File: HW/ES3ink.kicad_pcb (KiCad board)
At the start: 2 copper layers, 60.8 x 31 mm, 77 parts, among them J1 USB_C_Receptacle_USB2.0, J2 Conn_01x24_Pin, J3 Conn_01x02_Pin, J4 Conn_01x04_Socket, J5 USB_C_Receptacle_USB2.0, Q1 AO3401A, Q2 SI1308EDL-T1-GE3, Q3 DMP2045U-7, Q4 SI2305, SW1 RESET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

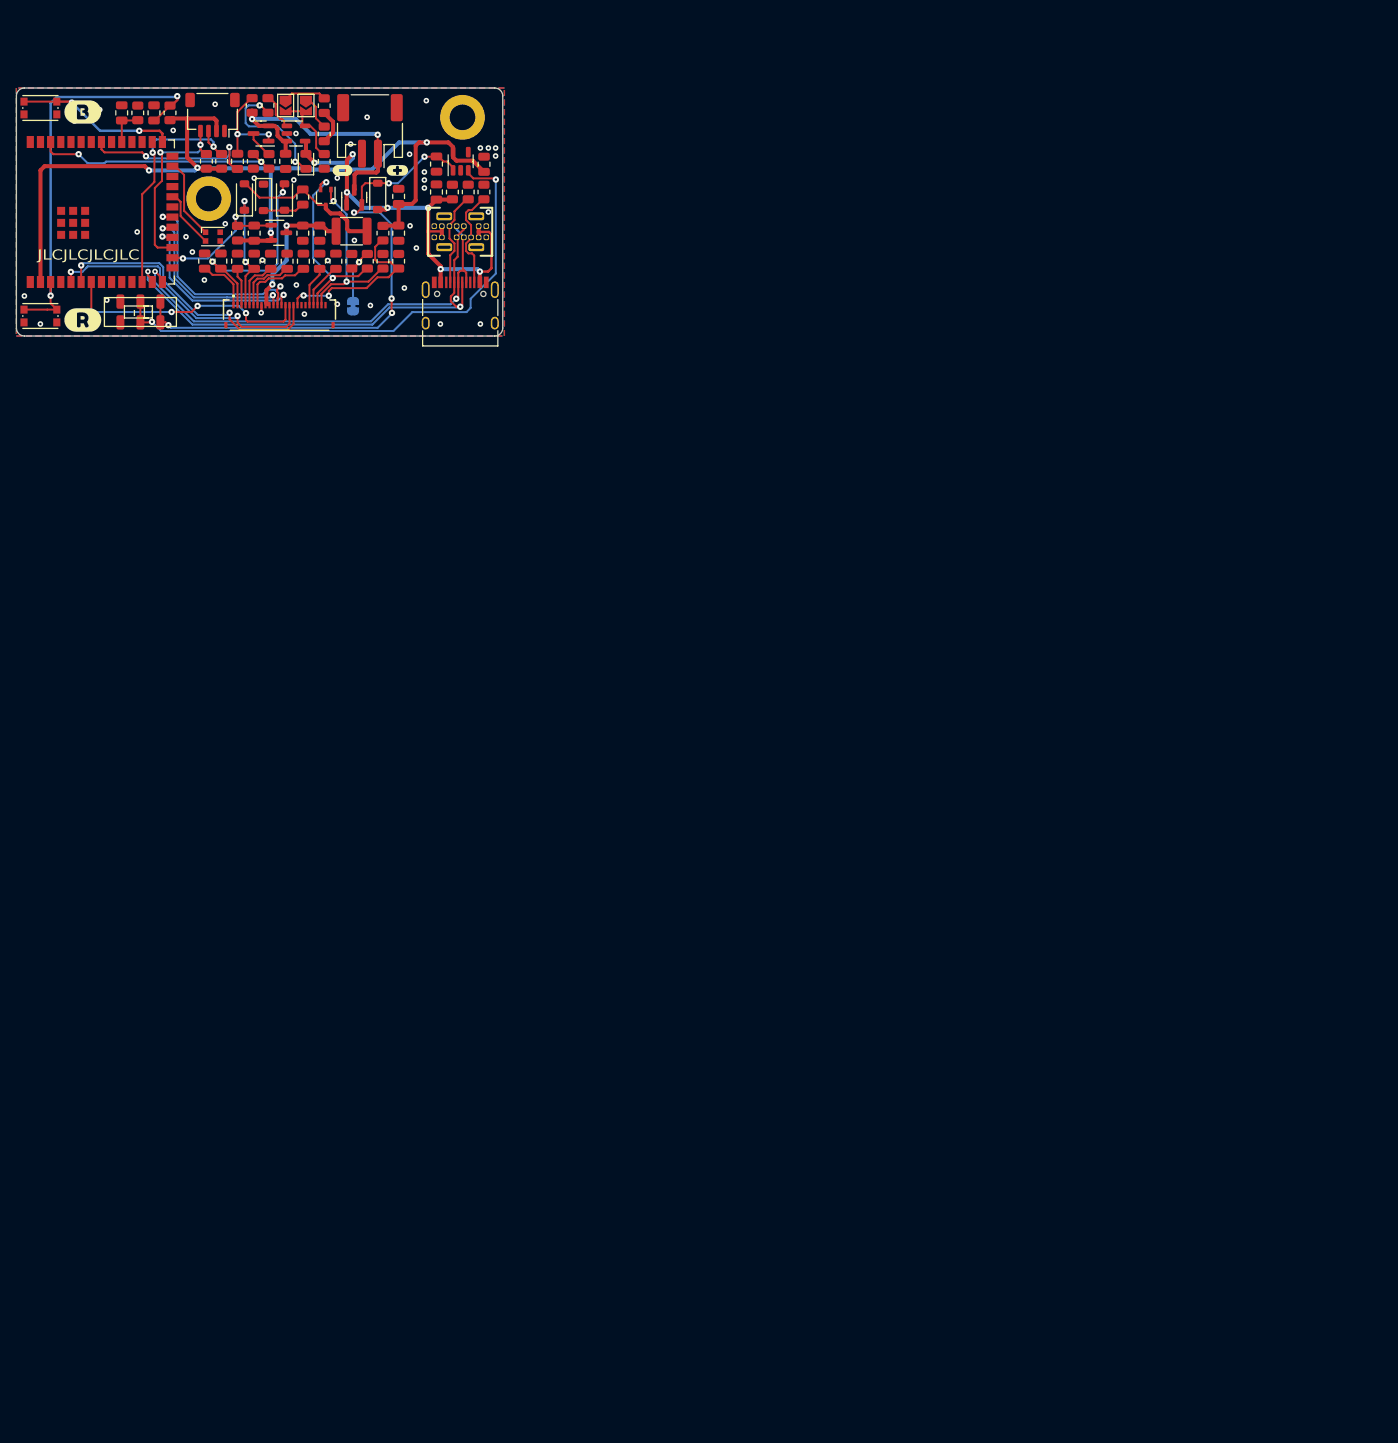
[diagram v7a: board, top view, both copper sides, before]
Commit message: Update to P1.2
- changed e-ink pwr pin to IO3
- unified reference text values
- add link to view design in KiCanvas
- version increment to P1.2
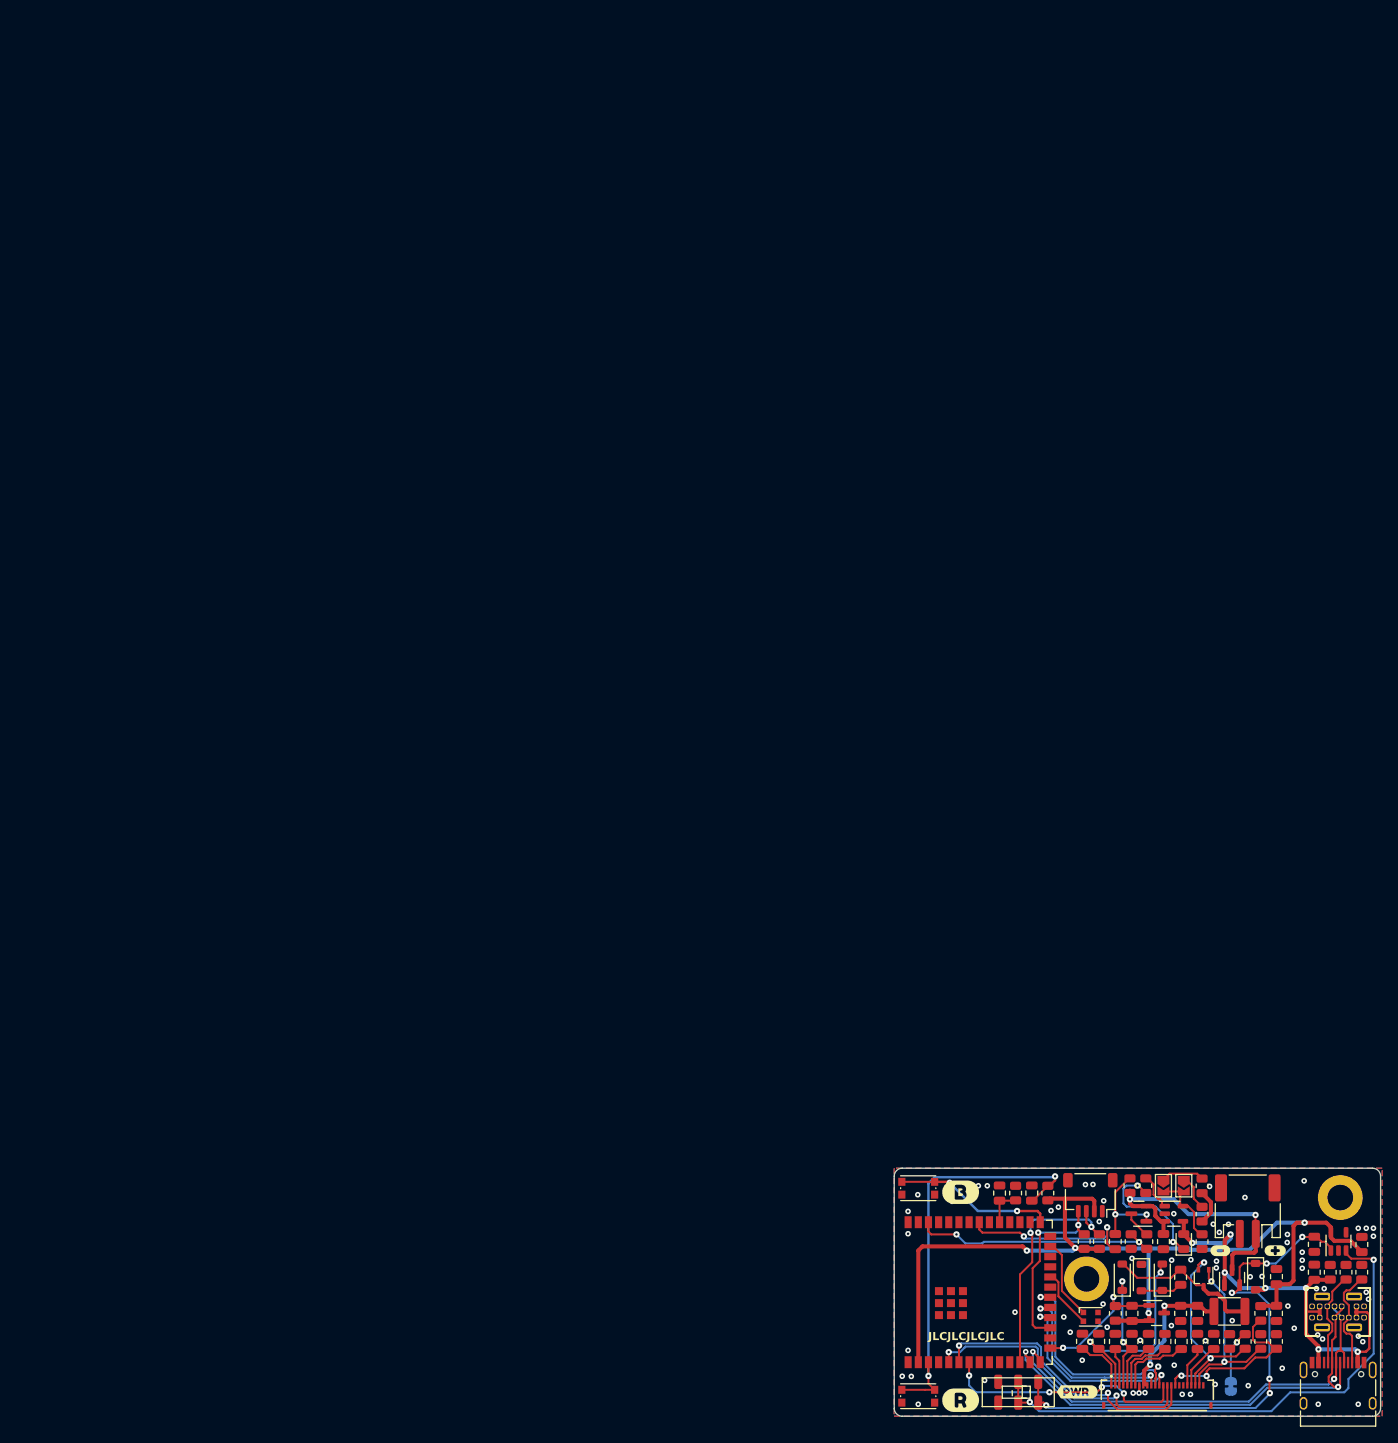
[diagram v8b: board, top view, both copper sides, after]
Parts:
- added kibuzzard-659DC4DE: G***, kibuzzard-659DC4DE, F.Cu at (132.6, 132.0)
- moved C19 174.0 mm to (145.5, 117.7)
- moved C21 174.0 mm to (162.2, 113.5)
- moved D1 174.0 mm to (138.2, 117.7)
- moved D2 174.0 mm to (143.2, 117.7)
- moved D3 174.0 mm to (140.6, 117.7)
- moved D6 174.0 mm to (134.3, 122.6)
- moved G*** 174.0 mm to (142.2, 120.0)
- moved G*** 174.0 mm to (154.1, 120.0)
- moved G*** 174.0 mm to (122.7, 120.0)
- moved J4 174.0 mm to (134.2, 107.4)
- moved Q3 174.0 mm to (152.0, 117.7)
- moved SW2 174.0 mm to (112.7, 106.5)
- moved U1 174.0 mm to (119.7, 119.5)
- moved kibuzzard-649216B3 174.0 mm to (118.0, 107.0)
- moved kibuzzard-64921EEB 174.0 mm to (150.5, 114.3)
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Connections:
- C13 pad 2: /IO46 -> /IO3
- Q1 pad 1: /IO46 -> /IO3
- R11 pad 2: /IO46 -> /IO3
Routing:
- net /IO3: track 0.00 -> 17.1 mm, vias 0 -> 2
- net /IO46: track 16.6 -> 0.00 mm, vias 2 -> 0
- net GND: vias 41 -> 71
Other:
- board text added: "P1.2"
- board text removed: "P1.1"
